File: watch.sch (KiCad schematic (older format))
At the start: 28 parts, among them P1 CONN_6, SW1 SW_PUSH, SW2 SW_PUSH, SW3 SW_PUSH, SW4 SW_PUSH, U1 nrf51822, U3 S25FL1-K, X1 16MHz, X2 32.768kHz

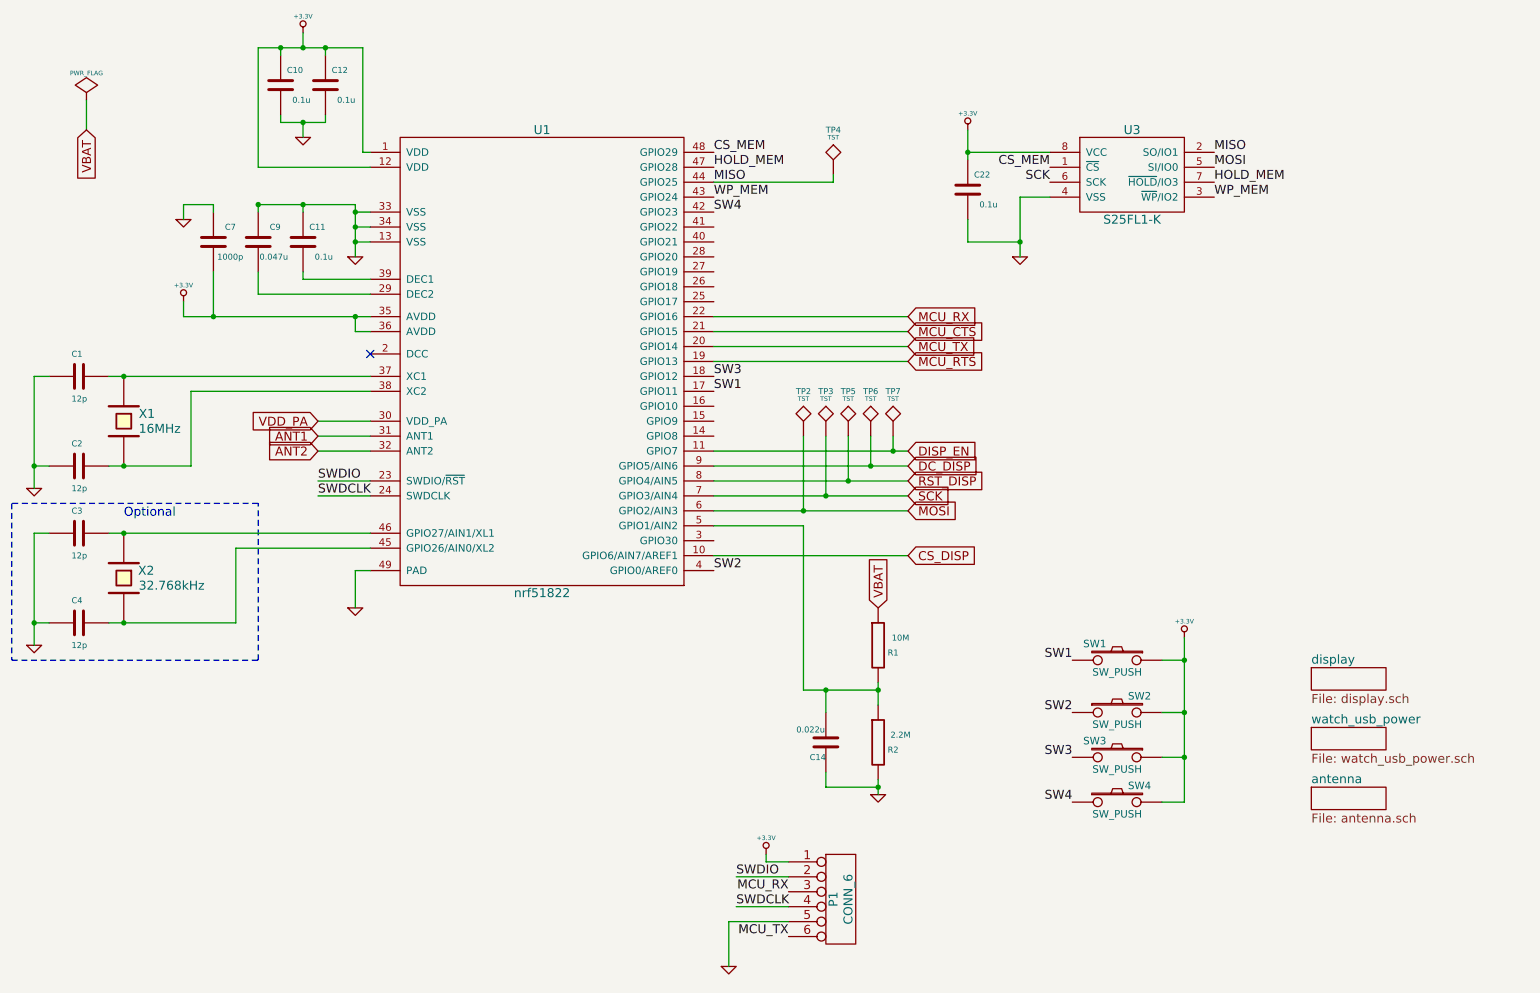
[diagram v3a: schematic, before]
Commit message: Fixed footprints for MCU and USB-UART, added testpoints
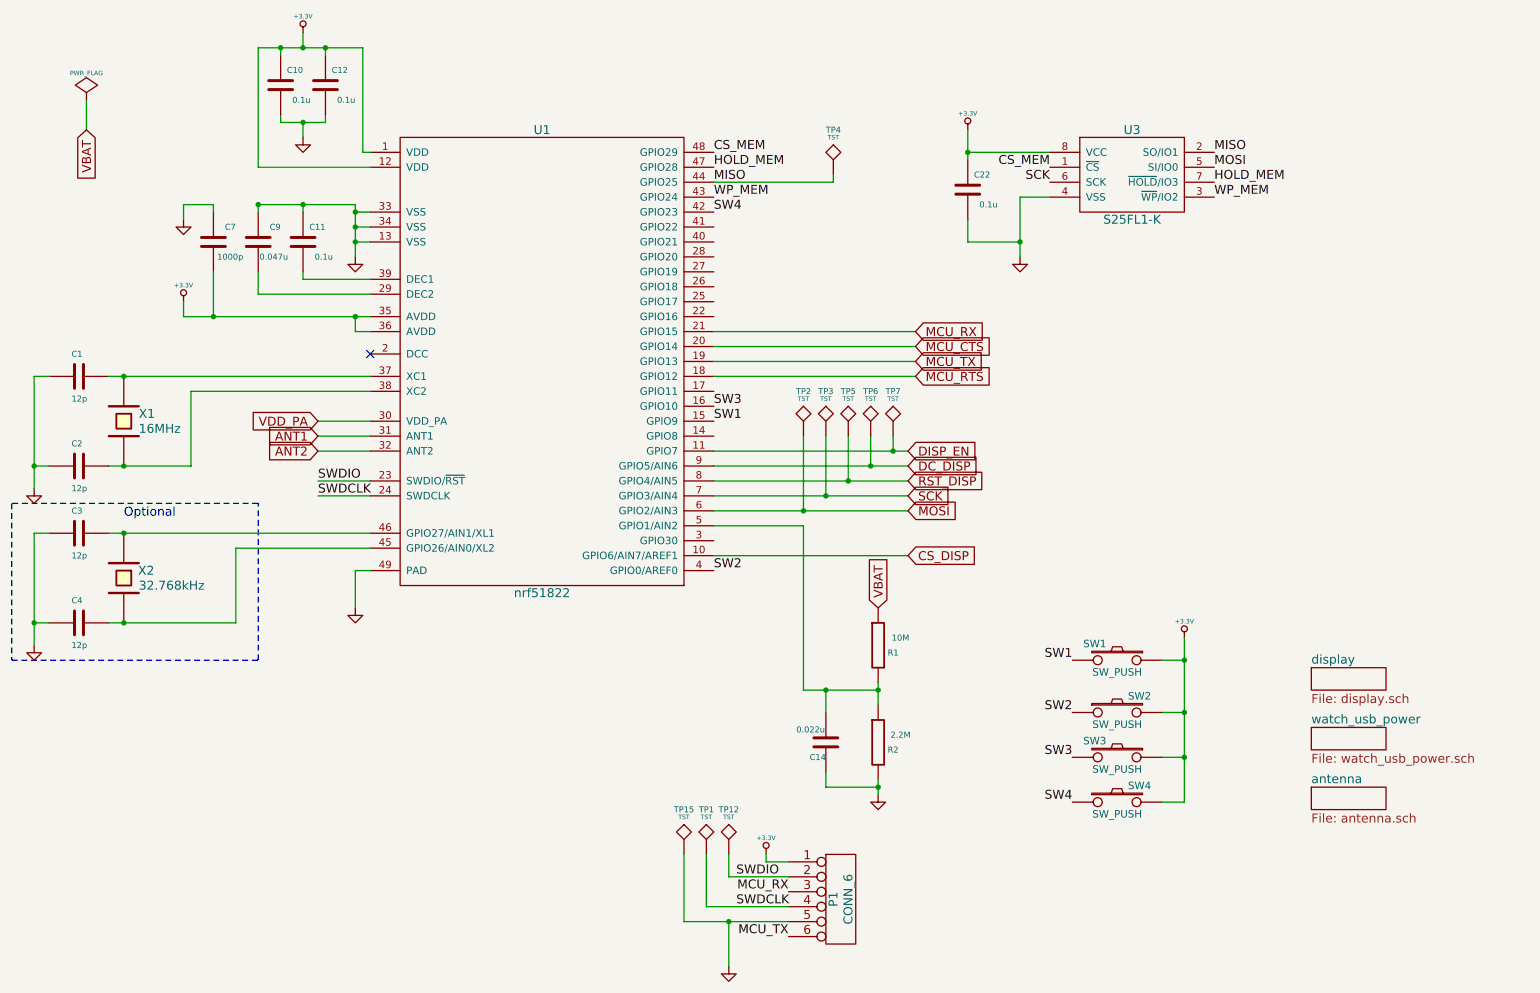
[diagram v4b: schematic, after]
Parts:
- added TP1, TP12, TP15: TST, Measurement_Points:Measurement_Point_Round-SMD-Pad_Small, symbol TST
- U1: footprint Housings_DFN_QFN:QFN-48-1EP_7x7mm_Pitch0.5mm -> Housings_QFN_DFN:UQFN-48-1EP_6x6mm_Pitch0.4mm
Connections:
- net GND: now also TP15.1
- net MCU_CTS: now also U1.20 (GPIO14); no longer U1.21 (GPIO15)
- net MCU_RTS: now also U1.18 (GPIO12); no longer U1.19 (GPIO13)
- net MCU_RX: now also U1.21 (GPIO15); no longer U1.22 (GPIO16)
- net MCU_TX: now also U1.19 (GPIO13); no longer U1.20 (GPIO14)
- net SW1: now also U1.15 (GPIO9); no longer U1.17 (GPIO11)
- net SW3: now also U1.16 (GPIO10); no longer U1.18 (GPIO12)
- net SWDCLK: now also TP1.1
- net SWDIO: now also TP12.1
